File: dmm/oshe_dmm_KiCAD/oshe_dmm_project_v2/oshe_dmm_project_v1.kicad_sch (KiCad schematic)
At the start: 83 parts, among them J1 FTDI Basic, J10 Voltage Range 2, J11 Voltage Range 3, J12 Voltage Range 3, J13 Current Indication, J2 Voltage, J3 GND, J4 Current, J5 Resistance Meas, J6 ON/OFF, J7 Voltage Range 1, J8 Voltage Range 1, J9 Voltage Range 2, SW1 PTS526 SK15 SMTR2 LFS, U1 ATmega328P-A, U2 INA219BxD, U3 ADS1115IDGS, U4 MAX4617CPE, U5 LM317_SOT-223, Y1 16MHz

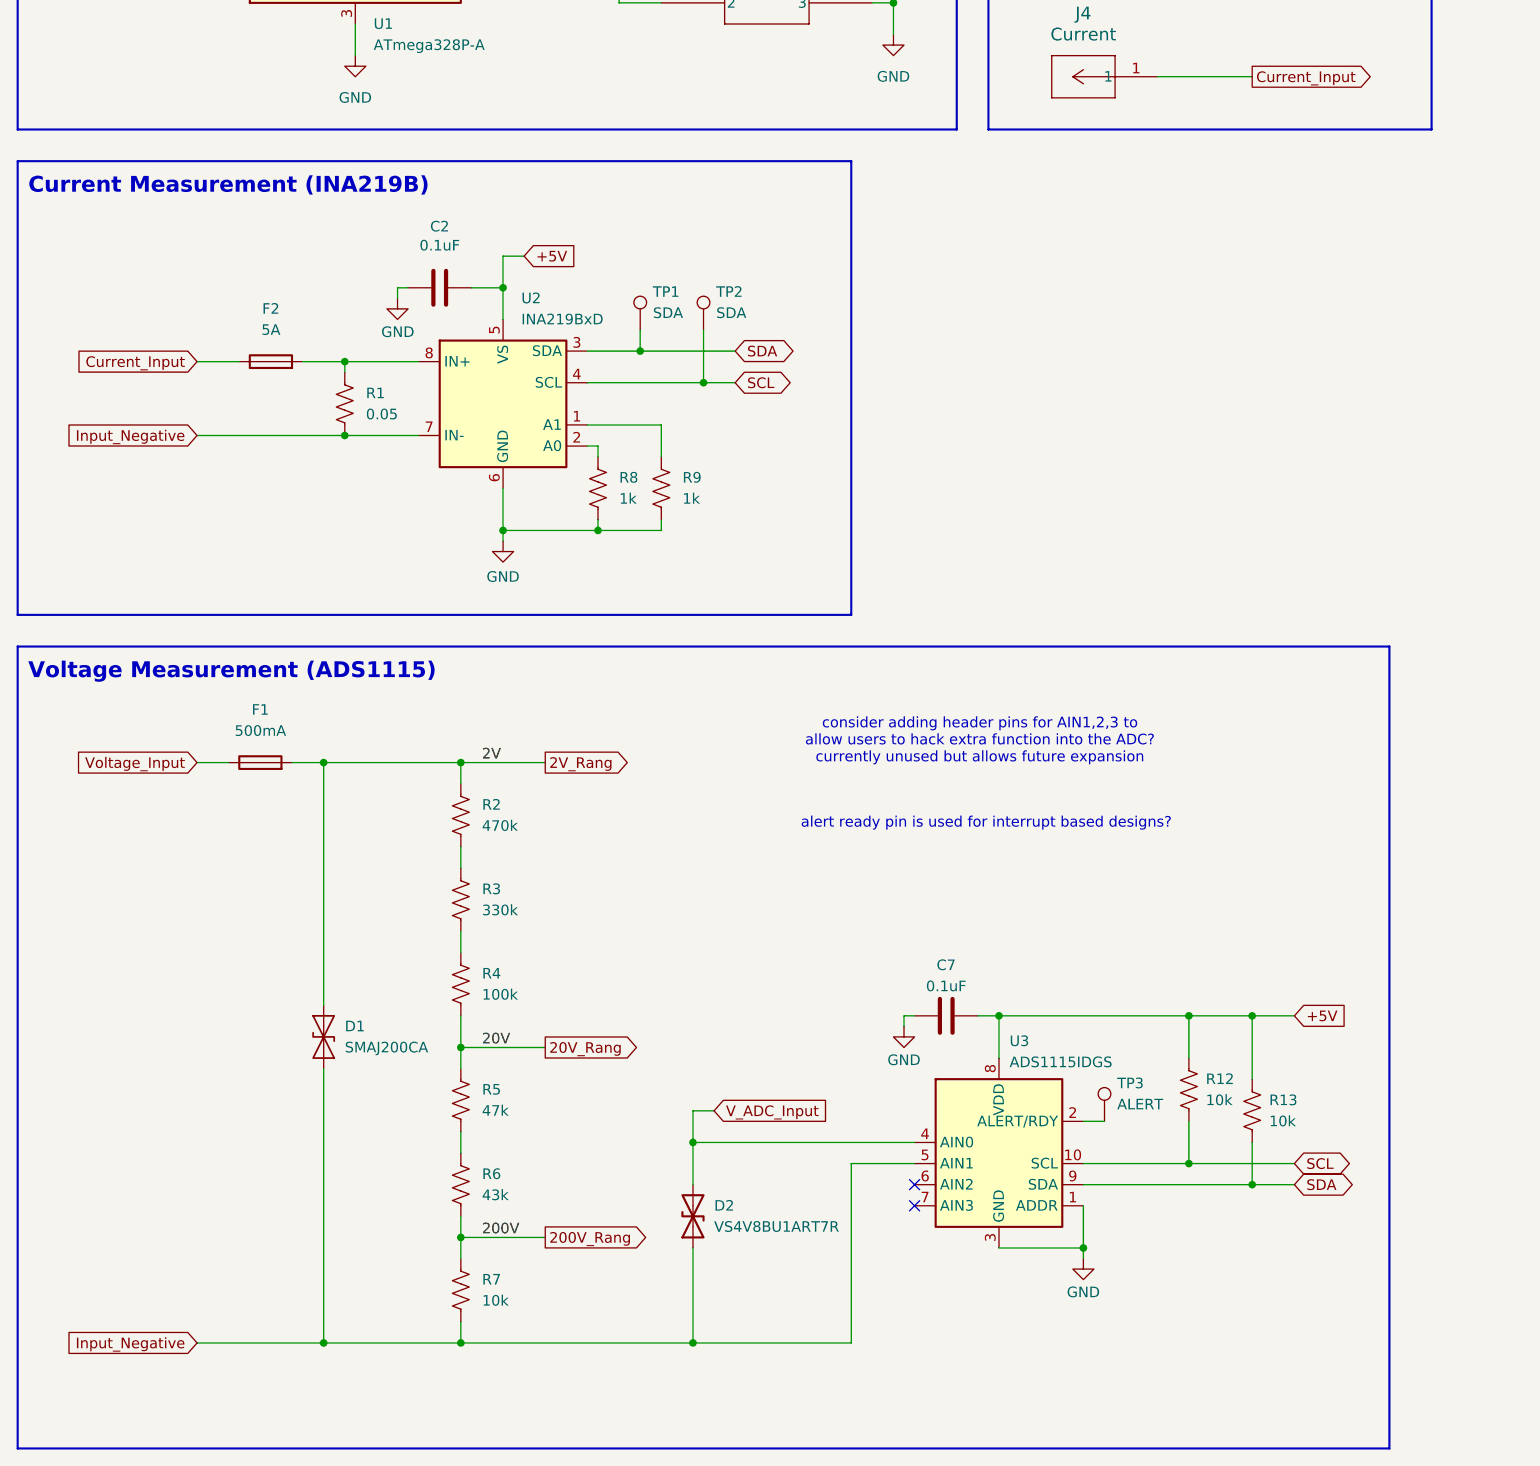
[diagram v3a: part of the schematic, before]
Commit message: Moved DC current measurement
Moved DC current measurement to use the same ADC as DC voltage measurement.
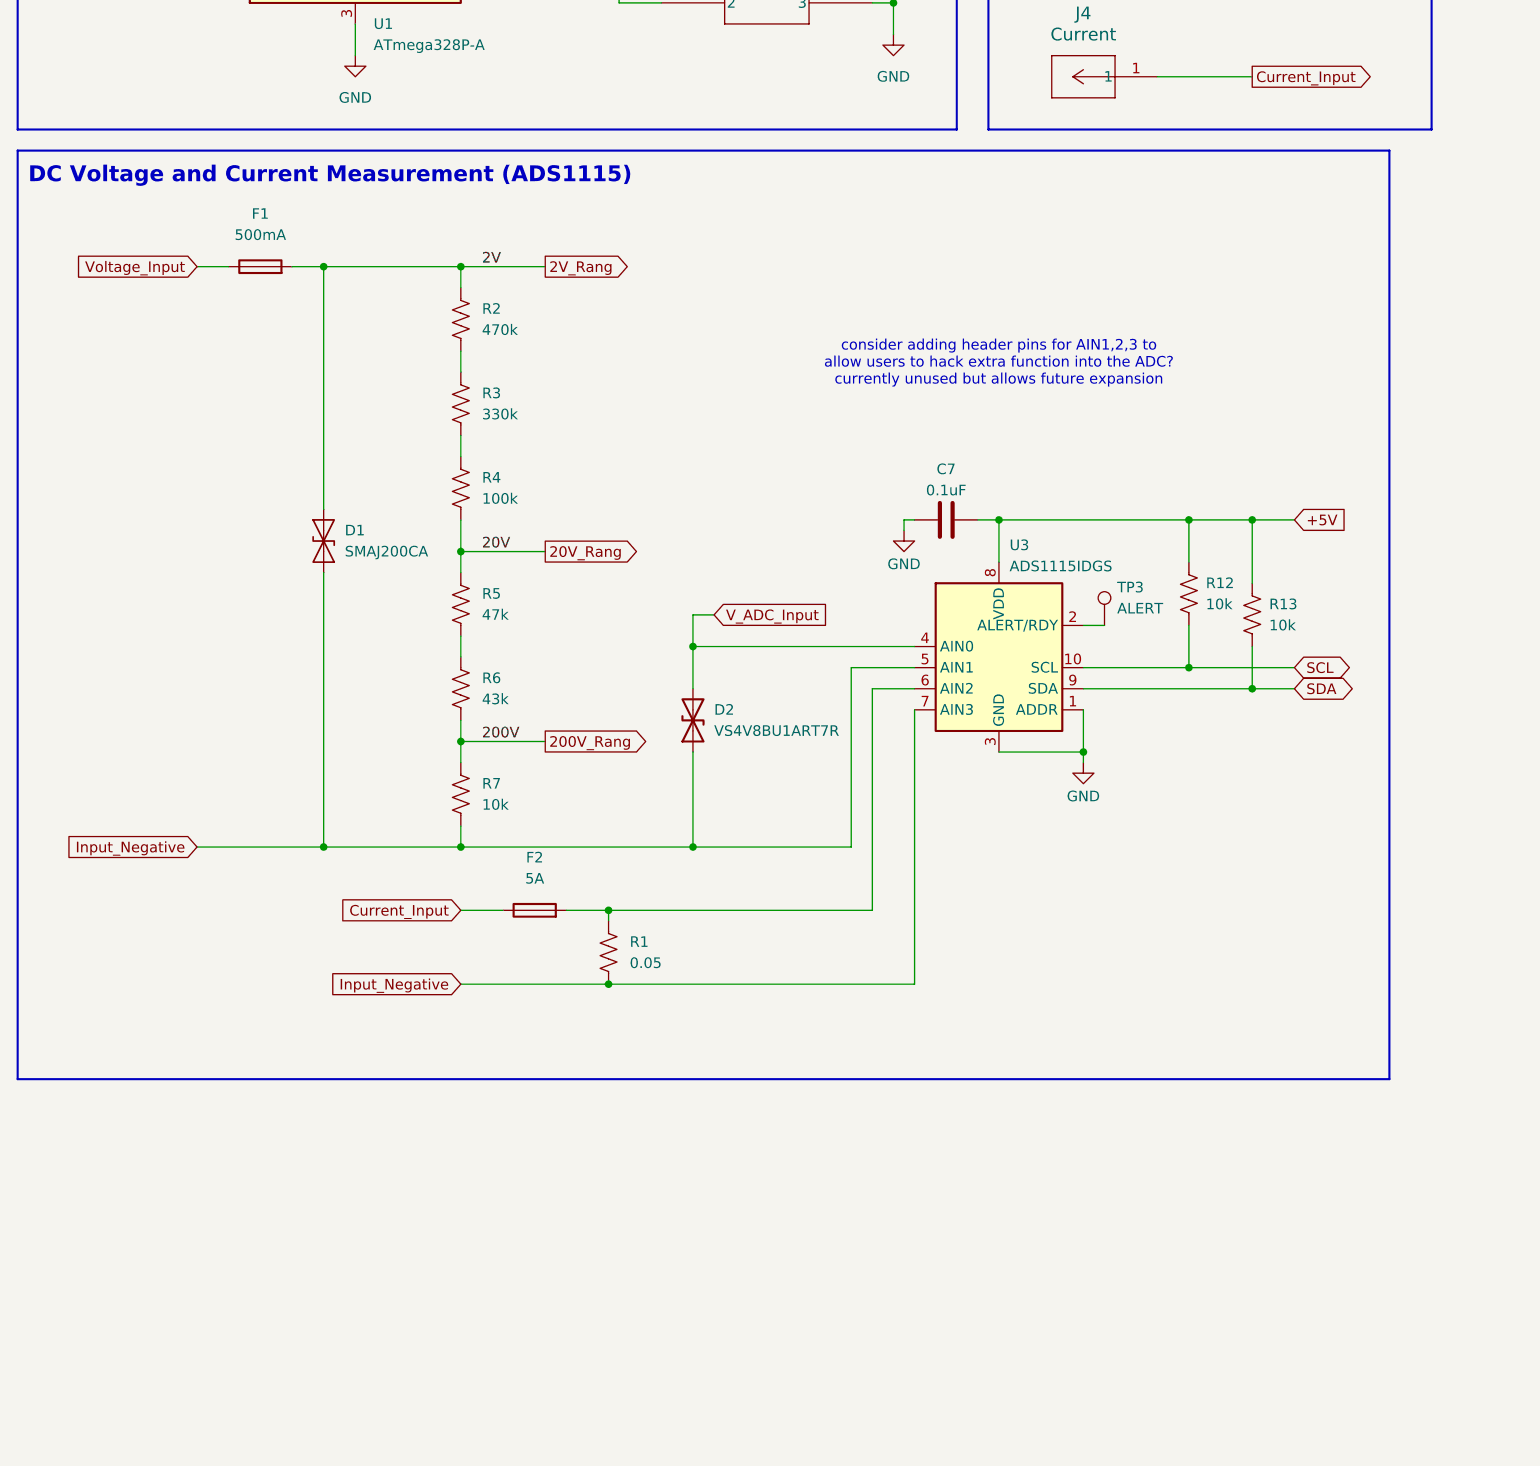
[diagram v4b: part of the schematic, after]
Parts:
- removed C2: 0.1uF, Capacitor_SMD:C_1206_3216Metric_Pad1.33x1.80mm_HandSolder, symbol Device:C
- removed R8, R9: 1k, Resistor_SMD:R_1206_3216Metric_Pad1.30x1.75mm_HandSolder, symbol Device:R_US
- removed TP1, TP2: SDA, TestPoint:TestPoint_Keystone_5019_Minature, symbol Connector:TestPoint
- removed U2: INA219BxD, Package_SO:SOIC-8_3.9x4.9mm_P1.27mm, symbol Sensor_Energy:INA219BxD
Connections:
- net GND: now also U3.7 (AIN3)
- net at F2.2, R1.1: now also U3.6 (AIN2)
- no-connect marks 8 -> 6
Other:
- note added: "DC Voltage and Current Measurement (ADS1115)"
- note removed: "Current Measurement (INA219B)"
- note removed: "Voltage Measurement (ADS1115)"
- note removed: "alert ready pin is used for interrupt based designs?"
- moved on the sheet: C7, D1, D2, F1, F2, R1, R12, R13, R2, R3, R4, R5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

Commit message: DC Voltage and Current Update
The PCB was updated so that only one ADC is used for DC voltage and current measurement. The footprint for the ADC was also updated.
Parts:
- U3: footprint Package_SO:TSSOP-10_3x3mm_P0.5mm -> ZC261500:MODULE_ZC261500
- U4: footprint DIP794W47P254L1943H457Q16 -> (none)
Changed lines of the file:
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@@
 			)
 		)
-		(property "Footprint" "DIP794W47P254L1943H457Q16"
+		(property "Footprint" ""
 			(at 261.62 123.19 0)
 			(effects
@@
 			)
 		)
-		(property "Footprint" "Package_SO:TSSOP-10_3x3mm_P0.5mm"
+		(property "Footprint" "ZC261500:MODULE_ZC261500"
 			(at 134.62 199.39 0)
 			(effects

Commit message: Updated PCB
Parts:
- added D7: SMAJ200A, Diode_SMD:D_SMA, symbol Diode:SMAJ200A
- added J14: Continuity, Connector_PinHeader_2.54mm:PinHeader_1x02_P2.54mm_Vertical, symbol Connector_Generic:Conn_01x02
- added J15, J16: AC Voltage Range 2, Connector_PinHeader_2.54mm:PinHeader_1x02_P2.54mm_Vertical, symbol Connector_Generic:Conn_01x02
- added J17, J18: AC Voltage Range 3, Connector_PinHeader_2.54mm:PinHeader_1x02_P2.54mm_Vertical, symbol Connector_Generic:Conn_01x02
- added J19, J20: AC Voltage Range 1, Connector_PinHeader_2.54mm:PinHeader_1x02_P2.54mm_Vertical, symbol Connector_Generic:Conn_01x02
- added J21: AC Current Indication, Connector_PinHeader_2.54mm:PinHeader_1x02_P2.54mm_Vertical, symbol Connector_Generic:Conn_01x02
- added R36: 2.4k, Resistor_SMD:R_1206_3216Metric_Pad1.30x1.75mm_HandSolder, symbol Device:R_US
- added R37: 3k, Resistor_SMD:R_1206_3216Metric_Pad1.30x1.75mm_HandSolder, symbol Device:R_US
- added R38: 1.8k, Resistor_SMD:R_1206_3216Metric_Pad1.30x1.75mm_HandSolder, symbol Device:R_US
- added R39, R9: R?, Resistor_SMD:R_1206_3216Metric_Pad1.30x1.75mm_HandSolder, symbol Device:R_US
- added R8: 1k, Resistor_SMD:R_1206_3216Metric_Pad1.30x1.75mm_HandSolder, symbol Device:R_US
- C9: footprint Connector_PinHeader_2.54mm:PinHeader_1x02_P2.54mm_Vertical -> Capacitor_THT:CP_Radial_D6.3mm_P2.50mm
- J13: value Current Indication -> DC Current Indication
- R22: value 390 -> 180
- R23: value 1k -> 680
- R24: value 1.78k -> 1.2k
- R25: value 3.3k -> R?
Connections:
- net +5V: now also J14.1 (Pin_1), J16.1 (Pin_1), J18.1 (Pin_1), J20.1 (Pin_1), J21.1 (Pin_1)
- net 200V_Rang: now also J17.1 (Pin_1)
- net 20V_Rang: now also J15.1 (Pin_1)
- net 2V_Rang: now also D7.1 (A1), J19.1 (Pin_1)
- net A1: now also D7.2 (A2)
- net A3: now also R36.1, R37.1, R38.1, R39.1, R8.2, R9.1
- net GND: now also R8.1
- net V_ADC_Input: now also J15.2 (Pin_2), J17.2 (Pin_2), J19.2 (Pin_2)
- new net: J21.2 (Pin_2), R39.2
- new net: J14.2 (Pin_2), R9.2
- new net: J16.2 (Pin_2), R36.2
- new net: J20.2 (Pin_2), R38.2
- new net: J18.2 (Pin_2), R37.2
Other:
- note added: "500-1000 ohm difference between settings detwermined bit value setting by writing code that reads analog pin and prints to serial monitor"
- note added: "ADC board size in 17mmX28mm"
- note added: "Continuity"
- note added: "Need to add another input to switching system for Rmeas Update cap footprint"
- note removed: "Need to add another input to switching system for Rmeas"
- moved on the sheet: C9, D4, J10, J11, J12, J13, J5, J7, J8, J9, R16, R17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

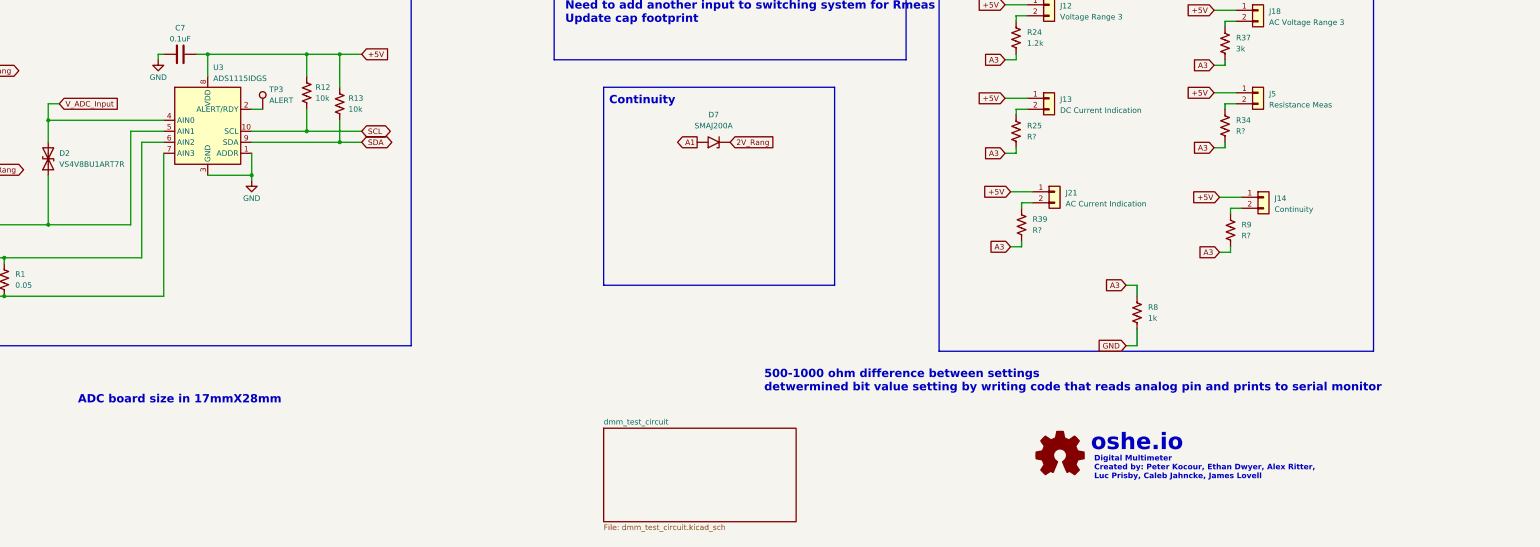
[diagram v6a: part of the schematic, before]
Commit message: AC current and voltage measurement
Updated Schematic and PCB to include AC voltage and current measurement. Also fixed an issue with DC voltage and current ADC had the wrong pin numbers assigned.
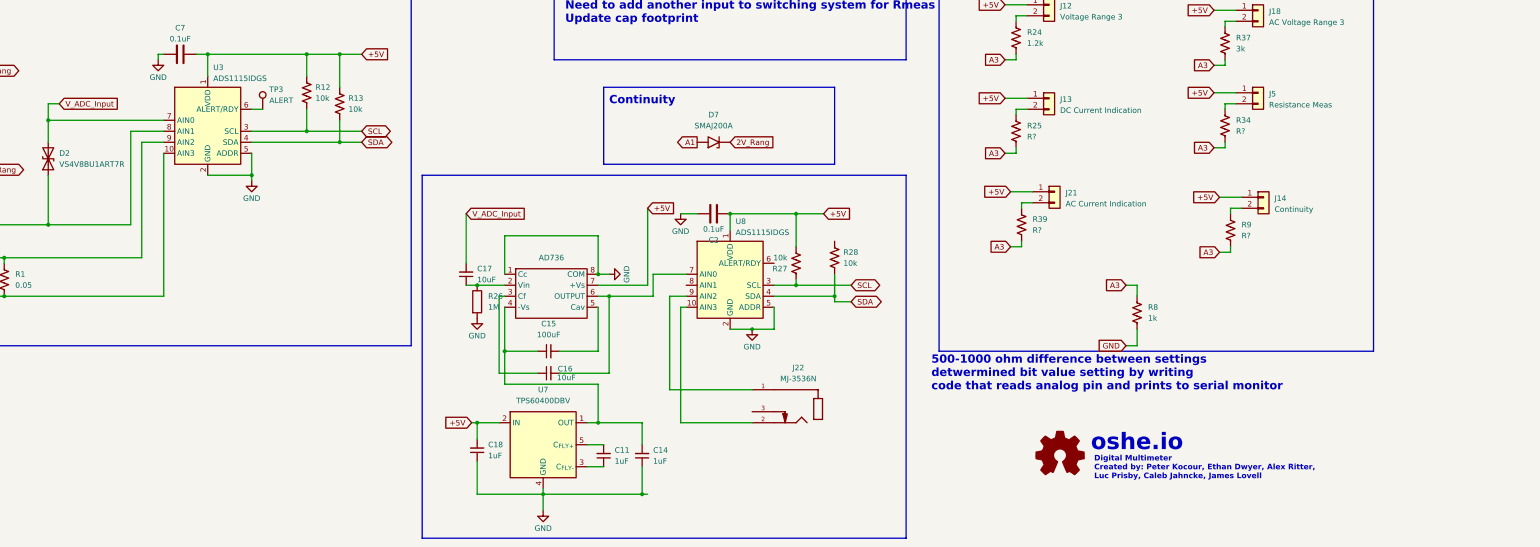
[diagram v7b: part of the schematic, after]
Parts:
- added C11, C14, C18: 1uF, Capacitor_SMD:CP_Elec_4x4.5, symbol Device:C_Small
- added C15: 100uF, footprints:CAPC3216X190N, symbol Device:C_Small
- added C16, C17: 10uF, Capacitor_SMD:C_1206_3216Metric_Pad1.33x1.80mm_HandSolder, symbol Device:C_Small
- added C2: 0.1uF, Capacitor_SMD:C_1206_3216Metric_Pad1.33x1.80mm_HandSolder, symbol Device:C
- added J22: MJ-3536N, footprints:SAMESKY_MJ-3536N, symbol MJ-3536N:MJ-3536N
- added R26: 1M, Resistor_SMD:R_1206_3216Metric_Pad1.30x1.75mm_HandSolder, symbol Device:R
- added R27, R28: 10k, Resistor_SMD:R_1206_3216Metric_Pad1.30x1.75mm_HandSolder, symbol Device:R_US
- added U2: AD736, footprints:PDIP-8_N, symbol cj_dmm:ad736
- added U7: TPS60400DBV, Package_TO_SOT_SMD:SOT-23-5, symbol Regulator_SwitchedCapacitor:TPS60400DBV
- added U8: ADS1115IDGS, ZC261500:MODULE_ZC261500, symbol Analog_ADC:ADS1115IDGS
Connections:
- net +5V: now also U3.1 (VDD), C18.2, C2.1, R27.2, U2.7 (+Vs), U7.2 (IN), U8.1 (VDD); no longer U3.8 (VDD)
- net GND: now also U3.10 (AIN3), U3.2 (GND), U3.8 (AIN1), C14.1, C18.1, C2.2, R26.2, U2.1 (Cc), U2.8 (COM), U7.4 (GND), U8.2 (GND), U8.5 (ADDR); no longer U3.1 (ADDR), U3.3 (GND), U3.7 (AIN3)
- net SCL: now also U3.3 (SCL), R27.1, U8.3 (SCL); no longer U3.10 (SCL)
- net SDA: now also U3.4 (SDA), R28.2, U8.4 (SDA); no longer U3.9 (SDA)
- net V_ADC_Input: now also U3.7 (AIN0), C17.2; no longer U3.4 (AIN0)
- net at F2.2, R1.1: now also U3.9 (AIN2); no longer U3.6 (AIN2)
- net at TP3.1: now also U3.6 (ALERT/RDY); no longer U3.2 (ALERT/RDY)
- new net: C14.2, C15.1, U2.4 (-Vs), U7.1 (OUT)
- new net: C17.1, R26.1, U2.2 (Vin)
- new net: C16.1, U2.3 (Cf)
- new net: C15.2, U2.5 (Cav)
- new net: C16.2, U2.6 (OUTPUT), U8.7 (AIN0)
- new net: J22.2, U8.10 (AIN3)
- new net: J22.1, U8.9 (AIN2)
- new net: C11.1, U7.3 (C_{FLY-})
- new net: C11.2, U7.5 (C_{FLY+})
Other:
- removed sheet dmm_test_circuit
- note removed: "ADC board size in 17mmX28mm"

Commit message: Finalished PCB
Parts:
- removed J15: AC Voltage Range 2, Connector_PinHeader_2.54mm:PinHeader_1x02_P2.54mm_Vertical, symbol Connector_Generic:Conn_01x02
- removed J17: AC Voltage Range 3, Connector_PinHeader_2.54mm:PinHeader_1x02_P2.54mm_Vertical, symbol Connector_Generic:Conn_01x02
- removed J19: AC Voltage Range 1, Connector_PinHeader_2.54mm:PinHeader_1x02_P2.54mm_Vertical, symbol Connector_Generic:Conn_01x02
- removed R27, R28: 10k, Resistor_SMD:R_1206_3216Metric_Pad1.30x1.75mm_HandSolder, symbol Device:R_US
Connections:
- net A1: no longer D7.2 (A2)
- net D10: now also D7.2 (A2)
